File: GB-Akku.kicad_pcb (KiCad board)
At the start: 2 copper layers, 35 x 30 mm, 61 parts, among them J1 Conn_01x01_Socket, J2 Conn_01x01_Socket, J3 Conn_01x01_Socket, J4 Conn_01x01_Socket, J5 Conn_01x04_Socket, Q1 PMV15ENEAR, Q2 PMV15ENEAR, U1 BQ25619, U2 BQ27546, U3 BQ297xy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

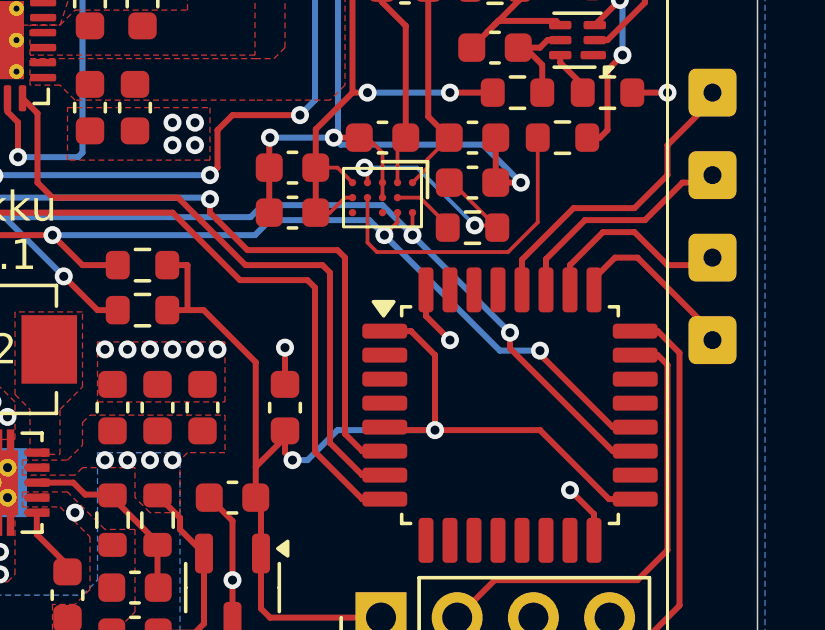
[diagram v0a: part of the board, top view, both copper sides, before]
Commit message: STM32 BOOT0 Pin fixed
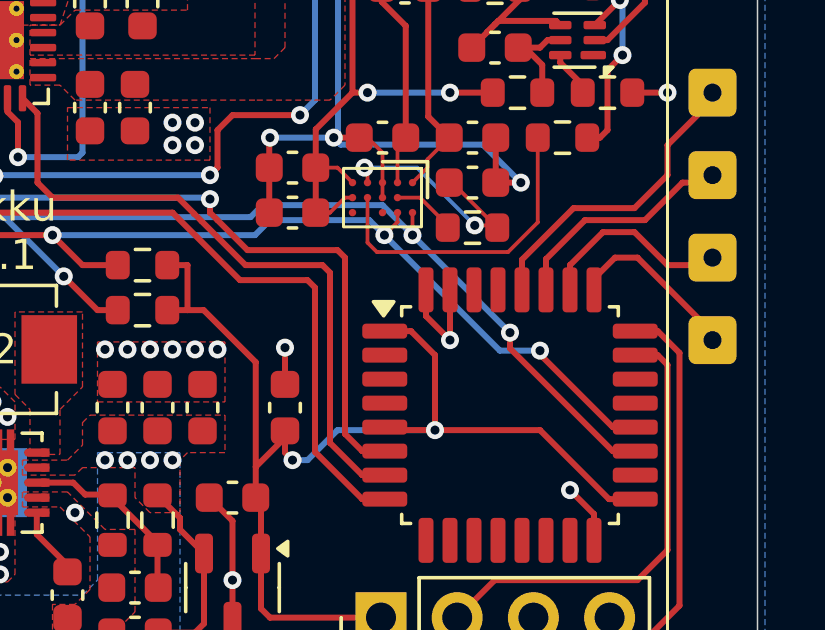
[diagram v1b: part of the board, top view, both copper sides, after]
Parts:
- U3: value BQ297xy -> BQ29737
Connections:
- U6 pad 31: unconnected-(U6-BOOT0-Pad31) -> GND
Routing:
- net GND: track 20.7 -> 22.4 mm
